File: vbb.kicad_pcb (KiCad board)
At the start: 2 copper layers, 49.5 x 49.5 mm, 18 parts, among them CON1 BARREL_JACK, J1 Screw_Terminal_1x02, J2 XM7D-0512, J3 CONN_02X02, J4 CONN_02X02, P1 CONN_02X01, P2 CONN_02X03, P3 CONN_02X04, P4 USB_B, P5 CONN_02X03, P6 USB_B, P7 USB_A, P8 CONN_02X03, P9 CONN_02X03

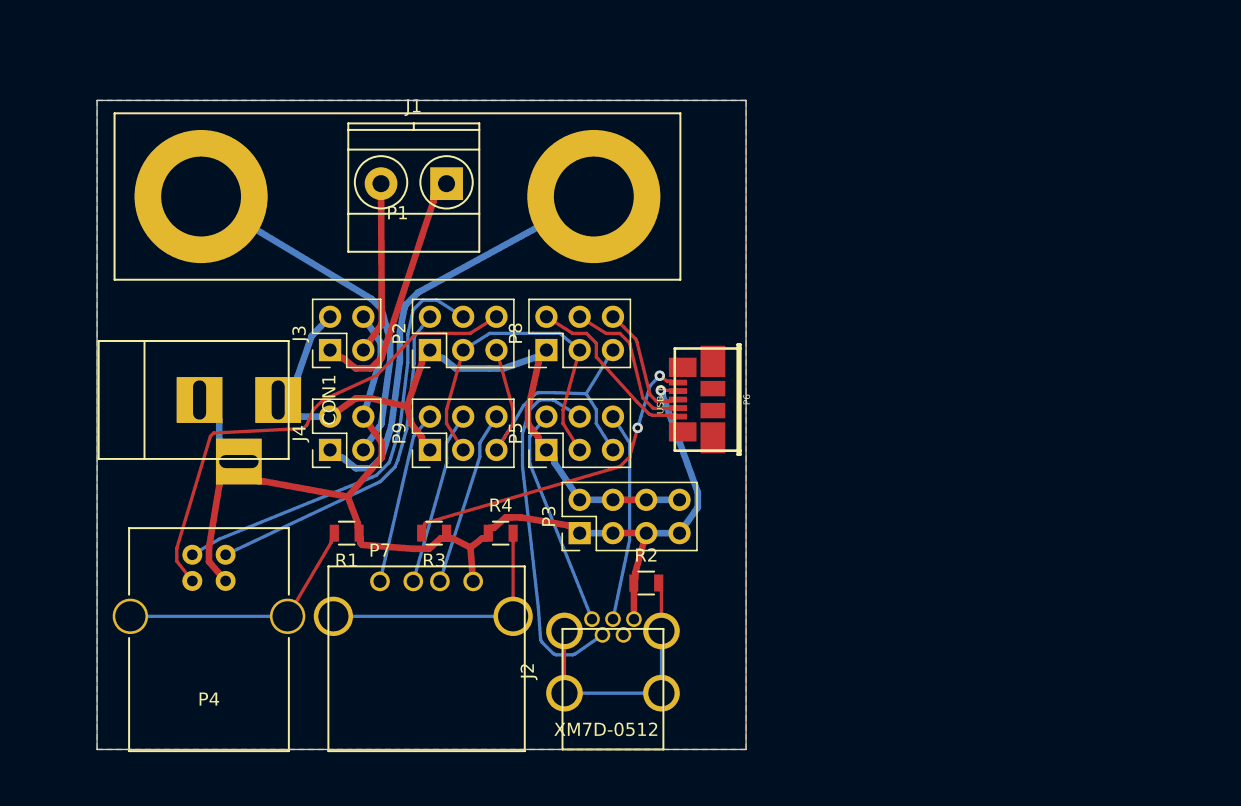
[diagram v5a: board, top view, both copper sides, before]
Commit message: Final (?) files. Swapped Banana jack pins on both PCB and schematics to have Red VCC, Black GND rendering. No actual layout change. Rearranged references on board Added VCC/GND marks on back side.
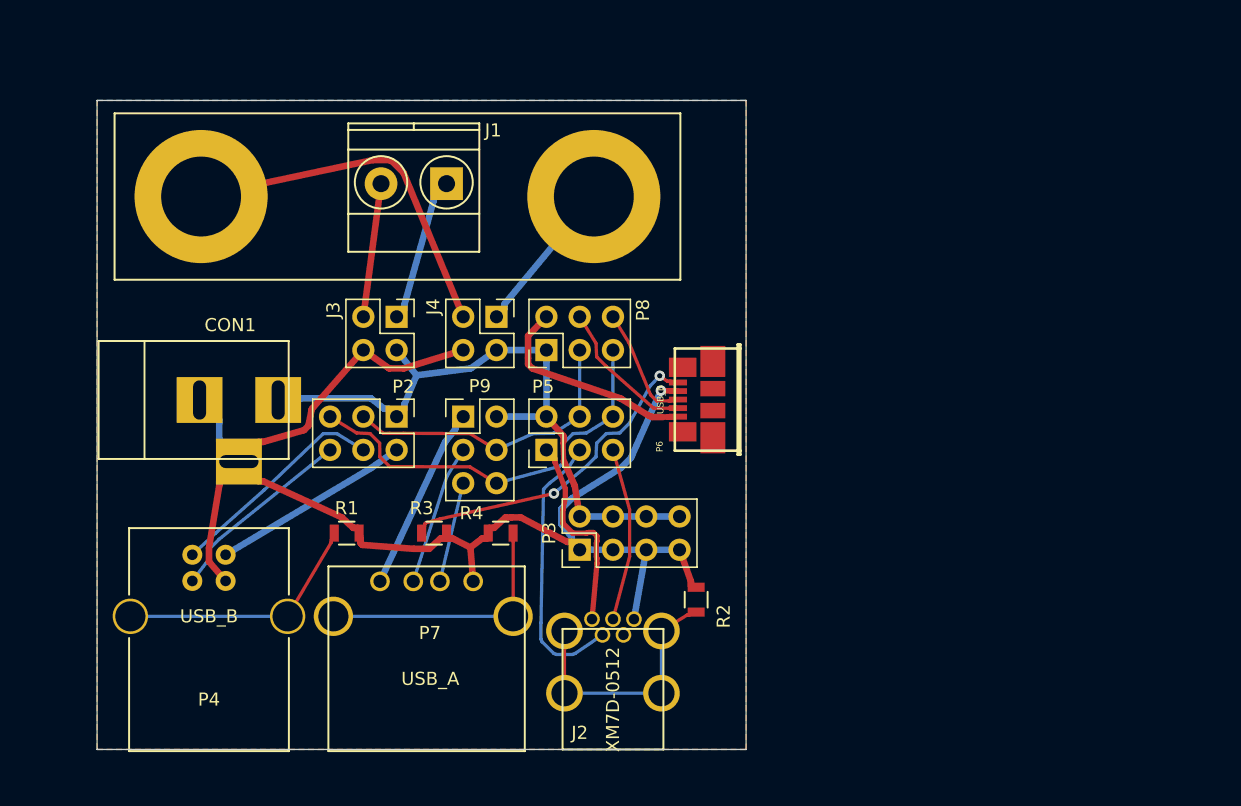
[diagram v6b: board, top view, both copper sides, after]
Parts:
- moved J4 16.3 mm to (96.5, 92.7), turned to 270 degrees
- moved J3 5.68 mm to (88.9, 92.7), turned to 270 degrees
- moved P2 5.68 mm to (88.9, 100.3), turned to 270 degrees
- moved R2 4.02 mm to (111.8, 114.3), turned to 270 degrees
- moved P9 3.59 mm to (94.0, 100.3), turned to 0 degrees
- moved P3 1.27 mm to (102.9, 110.5)
- turned P1 to 180 degrees
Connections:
- net Net-(P2-Pad2) renamed /VCC3
- net Net-(P6-Pad1) renamed /VCC5
- J2 pad 1: Net-(J2-Pad1) -> /VCC4
- P1 pad 1: /GND1 -> /VCC1
- P1 pad 2: /VCC1 -> /GND1
- P5 pad 1: /VCC -> /VCC4
- P5 pad 2: Net-(J2-Pad1) -> /VCC
- P5 pad 3: Net-(P2-Pad3) -> Net-(J2-Pad2)
- P5 pad 4: Net-(J2-Pad2) -> Net-(P2-Pad3)
- P5 pad 5: Net-(P2-Pad5) -> Net-(J2-Pad3)
- P5 pad 6: Net-(J2-Pad3) -> Net-(P2-Pad5)
- P7 pad 1: Net-(P7-Pad1) -> /VCC6
- P9 pad 1: /VCC -> /VCC6
- P9 pad 2: Net-(P7-Pad1) -> /VCC
- P9 pad 3: Net-(P2-Pad3) -> Net-(P7-Pad2)
- P9 pad 4: Net-(P7-Pad2) -> Net-(P2-Pad3)
- P9 pad 5: Net-(P2-Pad5) -> Net-(P7-Pad3)
- P9 pad 6: Net-(P7-Pad3) -> Net-(P2-Pad5)
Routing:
- net Net-(P2-Pad6): track 37.1 -> 14.7 mm
- net /VCC1: track 33.3 -> 11.9 mm
- net Net-(J2-Pad1): track 16.8 -> 0.00 mm
- net Net-(P2-Pad4): track 33.0 -> 17.0 mm
- net /VCC4: track 0.00 -> 15.4 mm
- net /VCC6: track 0.00 -> 14.2 mm
- net Net-(P7-Pad1): track 13.3 -> 0.00 mm
- net /GND: track 94.1 -> 105.7 mm
- net /VCC3: track 26.7 -> 15.3 mm
- net /VCC2: track 19.1 -> 11.1 mm
- net /VCC: track 57.7 -> 50.8 mm
- net Net-(J2-Pad2): track 27.9 -> 21.2 mm
- net Net-(P7-Pad3): track 13.4 -> 7.70 mm
- net Net-(P2-Pad5): track 26.1 -> 31.4 mm
- net Net-(P2-Pad3): track 26.0 -> 23.0 mm
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- added copper zone on B.Cu, net /GND
- added copper zone on F.Cu, net /VCC
- removed copper zone on F.Cu, net /GND
- removed copper zone on B.Cu, net /VCC
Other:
- net class VCC4 added: clearance 0.18, trace_width 0.4, via_dia 0.8, via_drill 0.4
- board text added: "GND"
- board text added: "VCC"

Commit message: Files as delivered for manufacturing.
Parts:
- added J5: CONN_01X01, Connectors:Banana_Jack_1Pin, F.Cu at (108.0, 83.8)
- added J6: CONN_01X01, Connectors:Banana_Jack_1Pin, F.Cu at (88.9, 83.8)
- J2: value XM7D-0512 -> Mini-B
- P1: value CONN_02X01 -> USB_A; footprint Connect:Banana_Jack_2Pin -> udif:MOLEX-48037-0001
- P6: value USB_B -> Micro_B
- moved P1 39.5 mm to (91.2, 123.0), turned to 0 degrees
- moved J1 21.6 mm to (71.1, 82.6), turned to 270 degrees
- moved J2 12.4 mm to (116.1, 119.4), turned to 270 degrees
- moved R2 11.4 mm to (101.1, 118.4)
- moved P4 6.99 mm to (75.7, 117.9), turned to 180 degrees
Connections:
- J4 pad 1: /VCC1 -> /GND1
- J4 pad 2: /VCC -> /GND
- J4 pad 3: /GND1 -> /VCC1
- J4 pad 4: /GND -> /VCC
- P1 pad 1: /VCC1 -> /VCC6
- P1 pad 2: /GND1 -> Net-(P1-Pad2)
- P7 pad 2: Net-(P7-Pad2) -> Net-(P1-Pad2)
- P7 pad 3: Net-(P7-Pad3) -> Net-(P1-Pad3)
- P7 pad 5: Net-(P7-Pad5) -> Net-(P1-Pad5)
- P9 pad 3: Net-(P7-Pad2) -> Net-(P1-Pad2)
- P9 pad 5: Net-(P7-Pad3) -> Net-(P1-Pad3)
- R4 pad 2: Net-(P7-Pad5) -> Net-(P1-Pad5)
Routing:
- net Net-(P1-Pad5): track 0.00 -> 35.1 mm
- net /GND: track 105.7 -> 127.4 mm
- net Net-(P7-Pad5): track 20.1 -> 0.00 mm
- net Net-(P1-Pad2): track 0.00 -> 19.0 mm
- net Net-(P1-Pad3): track 0.00 -> 15.9 mm
- net /VCC6: track 14.2 -> 29.3 mm
- net /GND1: track 28.0 -> 14.6 mm
- net Net-(P7-Pad2): track 10.8 -> 0.00 mm
- net /VCC2: track 11.1 -> 20.6 mm
- net Net-(P7-Pad3): track 7.70 -> 0.00 mm
- net Net-(P4-Pad5): track 19.3 -> 25.5 mm
- net /GND2: track 10.2 -> 16.1 mm
- net /VCC3: track 15.3 -> 20.0 mm
- net /VCC4: track 15.4 -> 19.5 mm
- net Net-(J2-Pad3): track 13.3 -> 17.3 mm
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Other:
- board text added: "https://github.com/udif/vbb"
- board text added: "© 2017 Udi Finkelstein"
- board text removed: "© 2017 Udi Finkelstein https://github.com/udif/vbb"
